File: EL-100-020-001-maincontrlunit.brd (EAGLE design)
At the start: 155.6 x 86 mm, 185 parts, among them T1 WS-TST-90°, U1 VNI4140K-32, U16 24AA256-I/SN, U19 ABS10-32.768KHZ-7-T, U2 VNI4140K-32, U3 VNI4140K-32, U8 MCP7940N-I/SN, U9 PMEG2005ET, X1 944-12-46-00, X10 S2L3.50/8/90G, X11 S2L3.50/8/90G, X12 S2L3.50/8/90G, X13 140-08-FLACHBAND1.27, X14 944-12-2-00, X2 944-12-46-00, X3 90G-14, X4 90G-14, X5 Q-063209, X6 Q-063209, X7 Q-063209, X8 Q-063209, X9 S2L3.50/8/90G

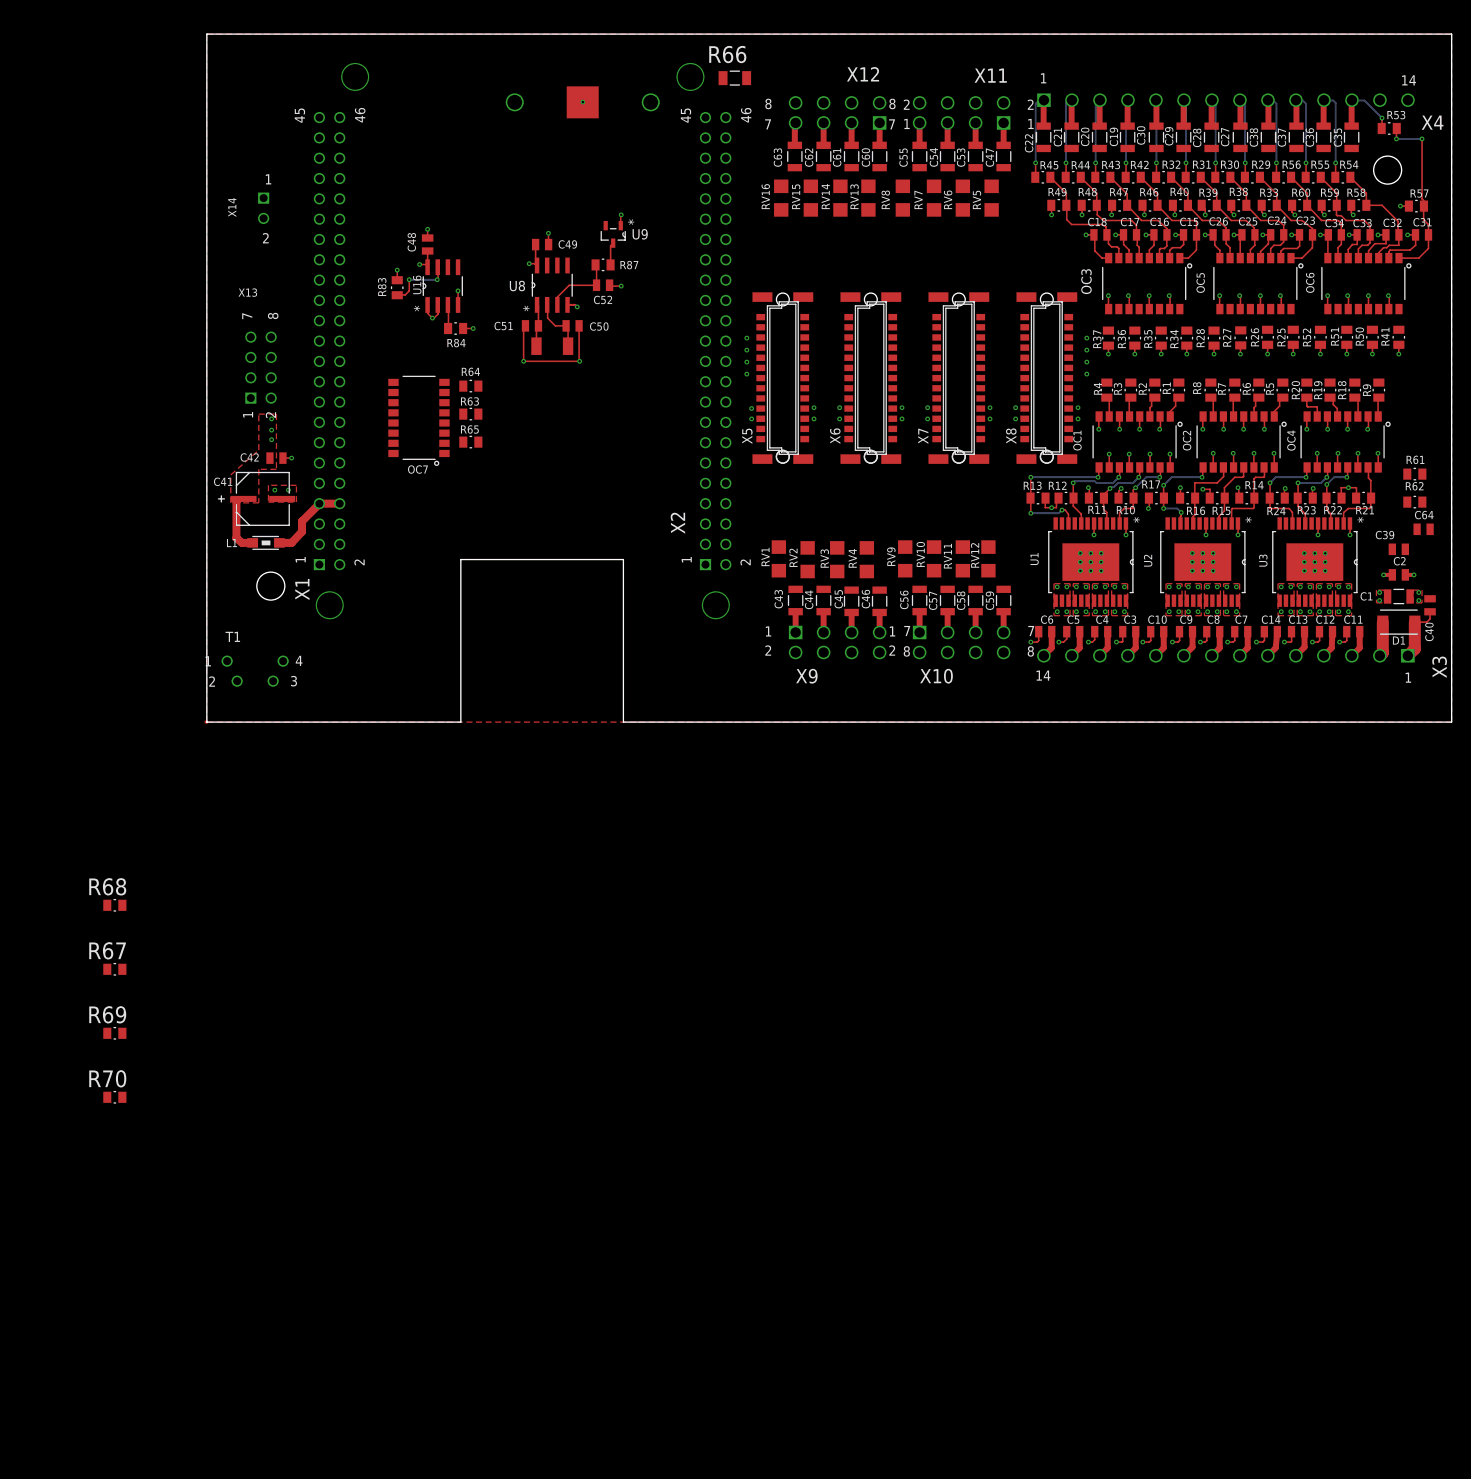
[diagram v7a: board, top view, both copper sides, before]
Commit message: update DIN rail
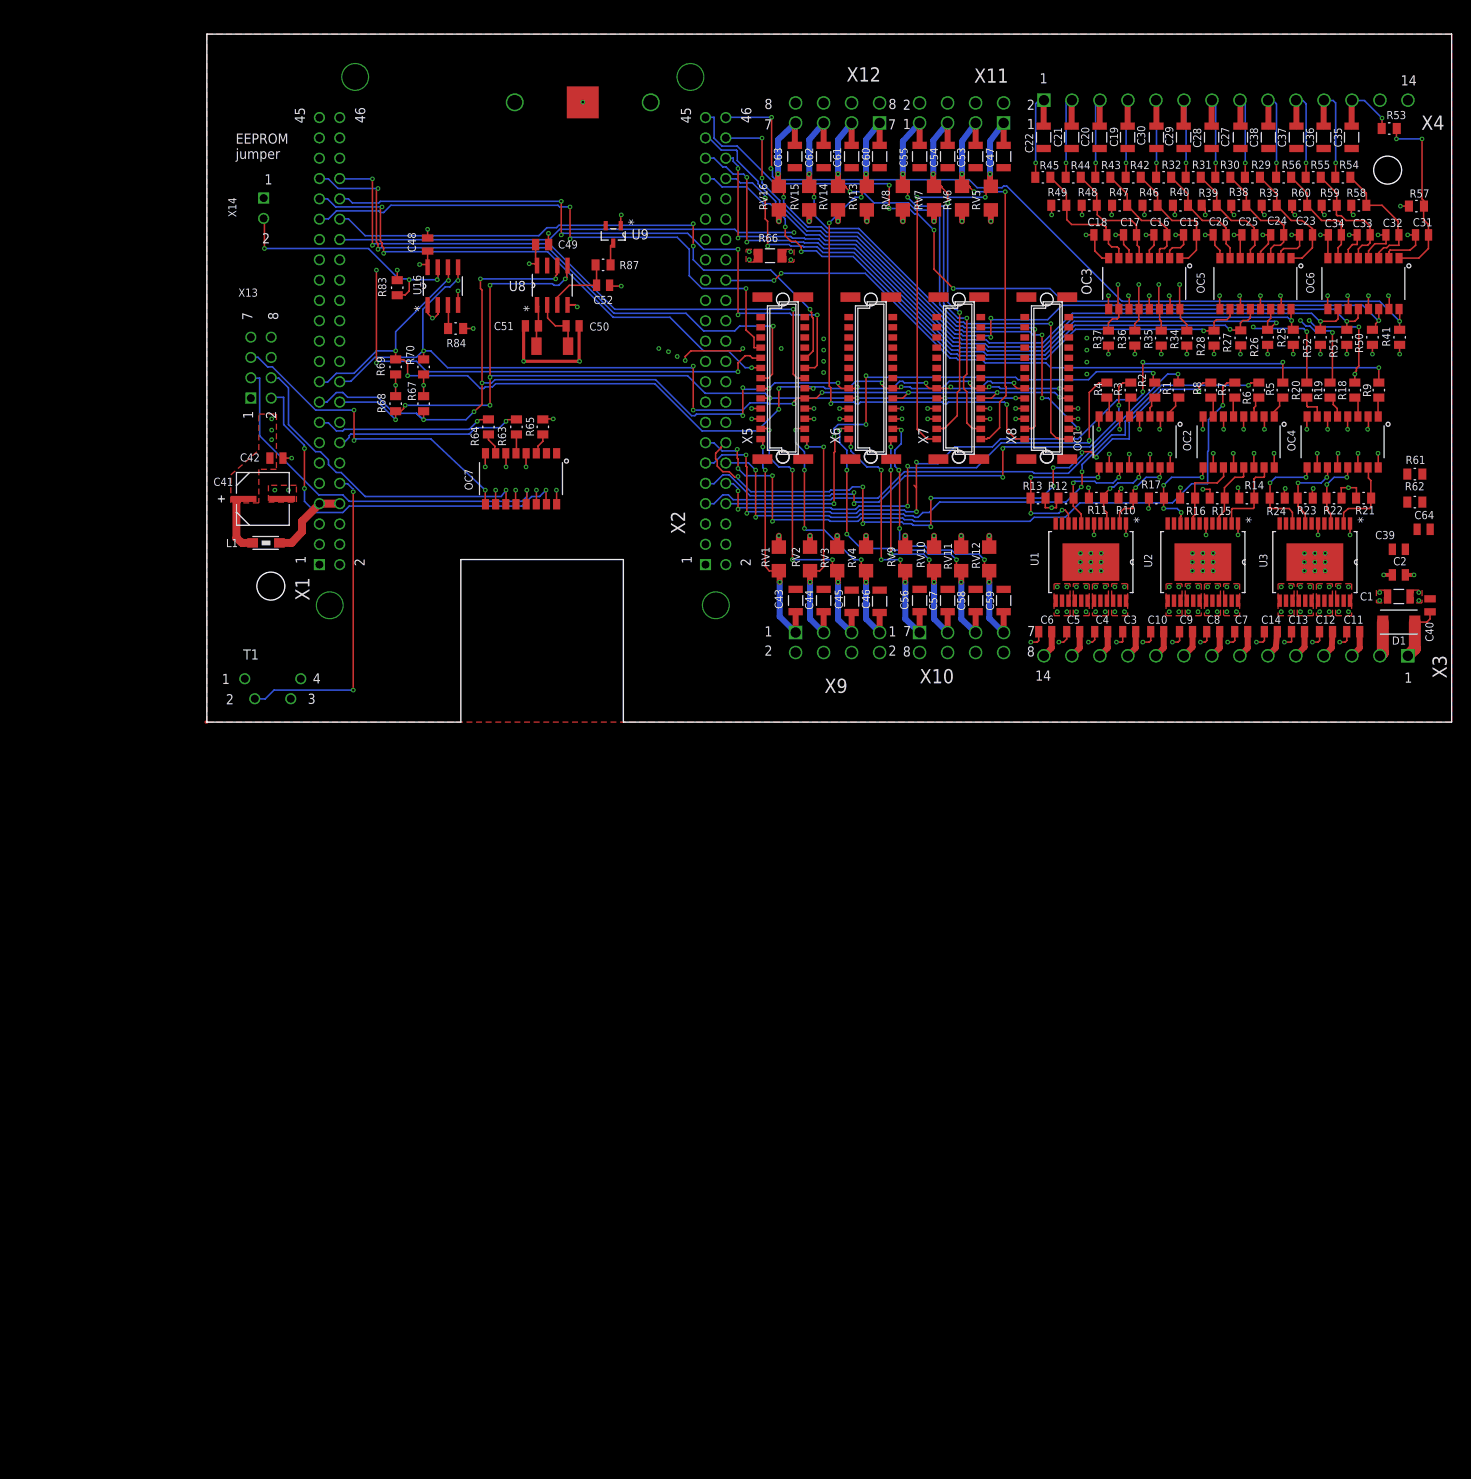
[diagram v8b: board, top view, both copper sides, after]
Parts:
- moved R70 99.1 mm to (27.1, 44.4), turned to 90 degrees
- moved R69 90.4 mm to (23.6, 44.4), turned to 90 degrees
- moved R67 80.6 mm to (27.1, 39.8), turned to 270 degrees
- moved R68 71.9 mm to (23.6, 39.8), turned to 270 degrees
- moved R66 22.6 mm to (70.4, 58.3)
- moved OC7 14.9 mm to (39.3, 30.4), turned to 270 degrees
- moved R65 9.20 mm to (42.0, 36.9), turned to 90 degrees
- moved R63 5.92 mm to (38.7, 36.9), turned to 270 degrees
- moved R64 5.55 mm to (35.2, 36.9), turned to 270 degrees
- moved T1 3.11 mm to (4.74, 5.42)
- moved RV2 0.32 mm to (75.4, 20.4)
- moved RV14 0.30 mm to (78.9, 65.5)
- moved RV16 0.30 mm to (71.5, 65.5)
- moved RV11 0.20 mm to (94.3, 20.4)
- moved RV13 0.20 mm to (82.5, 65.5)
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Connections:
- net +3.3V: now also R67.1, R68.1, R69.1, R70.1
- net I2C1_SCL: now also R67.2
- net I2C1_SDA: now also R68.2
- net I2C2_SCL: now also R69.2
- net I2C2_SDA: now also R70.2
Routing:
- net I2C1_SCL: track 0.00 -> 130.0 mm, vias 0 -> 13
- net I2C2_SCL: track 0.00 -> 122.4 mm, vias 0 -> 11
- net I2C1_SDA: track 0.00 -> 119.3 mm, vias 0 -> 10
- net I2C2_SDA: track 0.00 -> 119.1 mm, vias 0 -> 9
- net P8_45: track 0.00 -> 104.0 mm, vias 0 -> 5
- net P8_46: track 0.00 -> 102.3 mm, vias 0 -> 3
- net P8_29: track 0.00 -> 101.9 mm, vias 0 -> 3
- net P8_44: track 0.00 -> 99.3 mm, vias 0 -> 5
- net P8_11: track 0.00 -> 97.2 mm, vias 0 -> 7
- net P8_43: track 0.00 -> 95.2 mm, vias 0 -> 1
- net P8_28: track 0.00 -> 92.6 mm, vias 0 -> 2
- net P8_41: track 0.00 -> 92.4 mm, vias 0 -> 3
- net P8_15: track 0.00 -> 92.0 mm, vias 0 -> 2
- net P8_27: track 0.00 -> 91.1 mm, vias 0 -> 2
- net P8_42: track 0.00 -> 90.8 mm, vias 0 -> 3
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- added copper zone on layer 1, net AGND
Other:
- board text added: "EEPROM jumper"
